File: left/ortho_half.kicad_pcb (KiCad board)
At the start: 2 copper layers, 150.9 x 146.1 mm, 60 parts, among them J1 AudioJack4, J2 Conn_01x01, J3 Conn_01x01, J4 Conn_01x01, J5 Conn_01x01, J6 Conn_01x01, J7 Conn_01x01, J8 Conn_01x01, J9 Conn_01x01, K11 KEYSW_RGB, K12 KEYSW_RGB, K13 KEYSW_RGB, K14 KEYSW_RGB, K15 KEYSW_RGB, K16 KEYSW_RGB, K21 KEYSW_RGB, K22 KEYSW_RGB, K23 KEYSW_RGB, K24 KEYSW_RGB, K25 KEYSW_RGB, K26 KEYSW_RGB, K31 KEYSW_RGB, K32 KEYSW_RGB, K33 KEYSW_RGB, K34 KEYSW_RGB, K35 KEYSW_RGB, K36 KEYSW_RGB, K41 KEYSW_RGB, K42 KEYSW_RGB, K43 KEYSW_RGB, K44 KEYSW_RGB, K45 KEYSW_RGB, K46 KEYSW_RGB, K51 KEYSW_RGB, K52 KEYSW_RGB, K53 KEYSW_RGB, K54 KEYSW_RGB, K55 KEYSW_RGB, K56 KEYSW_RGB, K61 KEYSW_RGB, K62 KEYSW_RGB, K63 KEYSW_RGB, K64 KEYSW_RGB, K65 KEYSW_RGB, K66 KEYSW_RGB, SW1 SW_PUSH_RESET, U1 EliteC, U2 IS31FL3733-TQ

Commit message: Some initial work on the PCB update.
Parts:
- added SW2: Rotary_Encoder_Switch, Keebio-Parts:RotaryEncoder_Alps_EC11E-Switch_Vertical_H20mm, F.Cu at (143.2, 111.1)
- C1, C2, C3, C4, C5, C6: footprint Capacitor_Tantalum_SMD:CP_EIA-3216-10_Kemet-I_Pad1.58x1.35mm_HandSolder -> Capacitor_SMD:C_0805_2012Metric_Pad1.15x1.40mm_HandSolder; moved to B.Cu
- R1, R2, R3, R4, R5, Rext1: footprint Keebio-Parts:Resistor-Hybrid -> Resistor_SMD:R_0603_1608Metric_Pad1.05x0.95mm_HandSolder
- U1: value EliteC -> microctrl_superset; footprint Keebio-Parts:Elite-C-castellated-24pin-holes -> vladkvit_keyb:microcontroller_eliteC_ninenano
- moved C5 17.2 mm to (136.1, 89.7)
- moved Rext1 16.3 mm to (148.7, 83.5), turned to 0 degrees
- moved R3 12.3 mm to (148.7, 82.0), turned to 180 degrees
- moved C2 11.6 mm to (136.1, 91.6)
- moved C3 10.9 mm to (136.1, 99.3)
- moved R5 8.17 mm to (148.7, 80.5), turned to 180 degrees
- moved C1 6.07 mm to (136.1, 93.5)
- moved R2 4.13 mm to (148.7, 79.0), turned to 180 degrees
- moved R4 4.06 mm to (148.7, 76.0), turned to 0 degrees
- moved C4 3.46 mm to (136.1, 95.4)
- moved C6 1.87 mm to (136.1, 97.4)
- moved R1 0.20 mm to (148.7, 77.5), turned to 180 degrees
- turned U1 to 0 degrees
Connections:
- R1 pad 1: VCC -> VIO
- U1 pad 1: col7 -> col8
- U1 pad 10: serial -> col3
- U1 pad 13: INTB -> Net-(U1-Pad13)
- U1 pad 14: row6 -> serial
- U1 pad 15: row5 -> row6
- U1 pad 16: row4 -> row5
- U1 pad 17: row3 -> row4
- U1 pad 18: row2 -> row3
- U1 pad 19: row1 -> row2
- U1 pad 2: col6 -> col7
- U1 pad 20: Net-(U1-Pad20) -> row1
- U1 pad 24: VCC -> Net-(SW3-Pad2)
- U1 pad 7: col5 -> col6
- U1 pad 8: col4 -> col5
- U1 pad 9: col3 -> col4
- U2 pad 16: led_col6 -> (no net)
- U2 pad 17: led_col5 -> (no net)
- U2 pad 18: led_col4 -> led_col6
- U2 pad 19: led_col3 -> led_col5
- U2 pad 21: led_col2 -> led_col4
- U2 pad 22: led_col1 -> led_col3
- U2 pad 23: (no net) -> led_col2
- U2 pad 24: (no net) -> led_col1
- U2 pad 25: led_col14 -> (no net)
- U2 pad 26: led_col13 -> (no net)
- U2 pad 27: led_col12 -> led_col14
- U2 pad 28: led_col11 -> led_col13
- U2 pad 30: led_col10 -> led_col12
- U2 pad 31: led_col9 -> led_col11
- U2 pad 32: (no net) -> led_col10
- U2 pad 33: (no net) -> led_col9
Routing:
- net GND: track 161.7 -> 110.8 mm, vias 45 -> 29
- net VCC: track 160.5 -> 119.6 mm, vias 1 -> 0
- net INTB: track 47.0 -> 11.2 mm, vias 1 -> 0
- net serial: track 21.8 -> 1.78 mm, vias 1 -> 0
- net Net-(Rext1-Pad1): track 22.0 -> 3.30 mm, vias 2 -> 0
- net encA2: track 0.00 -> 9.52 mm
- net encA1: track 0.00 -> 9.52 mm
- net Net-(U1-Pad27): track 0.00 -> 9.52 mm
- net SCL: track 69.2 -> 76.5 mm
- net SDA: track 77.0 -> 82.4 mm
- net col6: track 141.8 -> 138.7 mm
- net led_col4: track 113.2 -> 115.9 mm
- net led_col3: track 132.5 -> 135.2 mm
- net col4: track 165.0 -> 167.6 mm
- net col3: track 187.9 -> 190.5 mm
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
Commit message: More PCB updates
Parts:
- added J10: Conn_01x04, Connector_PinHeader_2.54mm:PinHeader_1x04_P2.54mm_Vertical, F.Cu at (159.4, 51.8)
- added J11: Conn_01x02, Connector_JST:JST_PH_S2B-PH-K_1x02_P2.00mm_Horizontal, F.Cu at (162.8, 60.4)
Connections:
- U1 pad 30: (no net) -> VBUS
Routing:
- net VCC: track 119.6 -> 92.3 mm
- net SDA: track 82.4 -> 65.9 mm
- net SCL: track 76.5 -> 63.7 mm
- net INTB: track 11.2 -> 3.99 mm
- net SDB: track 6.41 -> 3.90 mm

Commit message: More PCB stuff
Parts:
- R1, R2, R3, R4, R5, Rext1: moved to B.Cu
- SW2: footprint Keebio-Parts:RotaryEncoder_Alps_EC11E-Switch_Vertical_H20mm -> vladkvit_keyb:RotaryEncoderEC11_MX_combo
- moved J11 32.4 mm to (130.5, 59.0)
- moved J10 21.3 mm to (138.2, 53.2)
- moved C3 8.00 mm to (131.9, 92.5)
- moved Rext1 7.96 mm to (147.7, 75.6)
- moved R4 7.05 mm to (147.7, 83.0)
- moved R3 5.02 mm to (147.7, 77.0)
- moved R1 4.13 mm to (147.7, 81.5)
- moved J1 3.45 mm to (153.7, 60.0)
- moved R5 2.18 mm to (147.7, 78.5)
- moved R2 1.43 mm to (147.7, 80.0)
- moved SW2 0.45 mm to (143.5, 110.7)
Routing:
- net SDA: track 65.9 -> 71.5 mm
- net GND: track 110.5 -> 115.9 mm
- net SCL: track 63.7 -> 69.1 mm
- net VCC: track 92.3 -> 95.0 mm
- net VIO: track 67.4 -> 65.5 mm, vias 4 -> 0
- net row6: track 254.3 -> 255.7 mm
- net col1: track 228.9 -> 228.2 mm
- net row5: track 187.9 -> 188.6 mm
- net led_row3B: track 389.1 -> 388.4 mm
- net row4: track 170.0 -> 170.7 mm
- net led_row3A: track 403.3 -> 402.7 mm
- net led_row3C: track 379.4 -> 378.9 mm

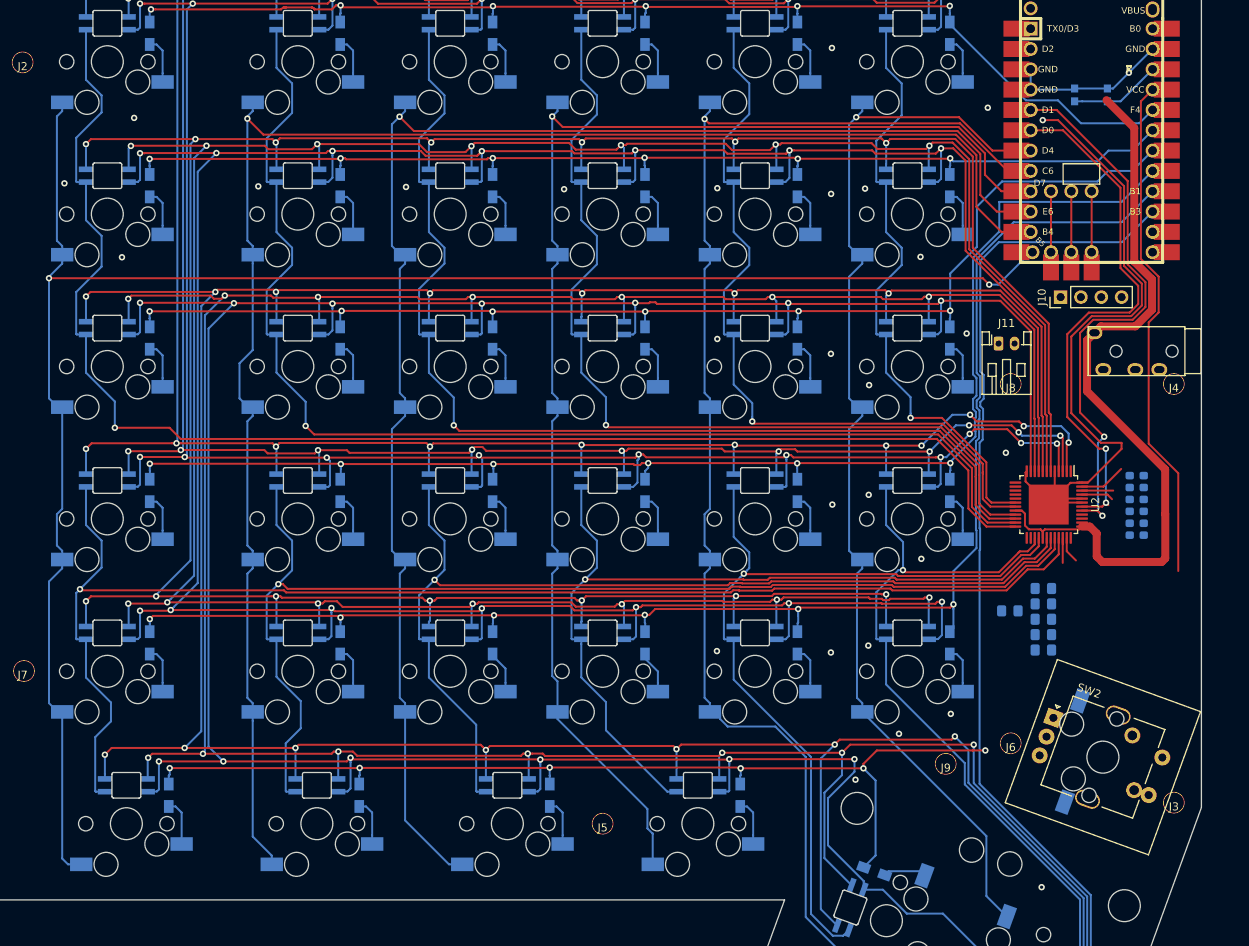
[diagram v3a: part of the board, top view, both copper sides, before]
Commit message: A bunch of changes to left half of PCB in order to make room for battery and various connectors. Also added a switch and extra connector on the schematic.
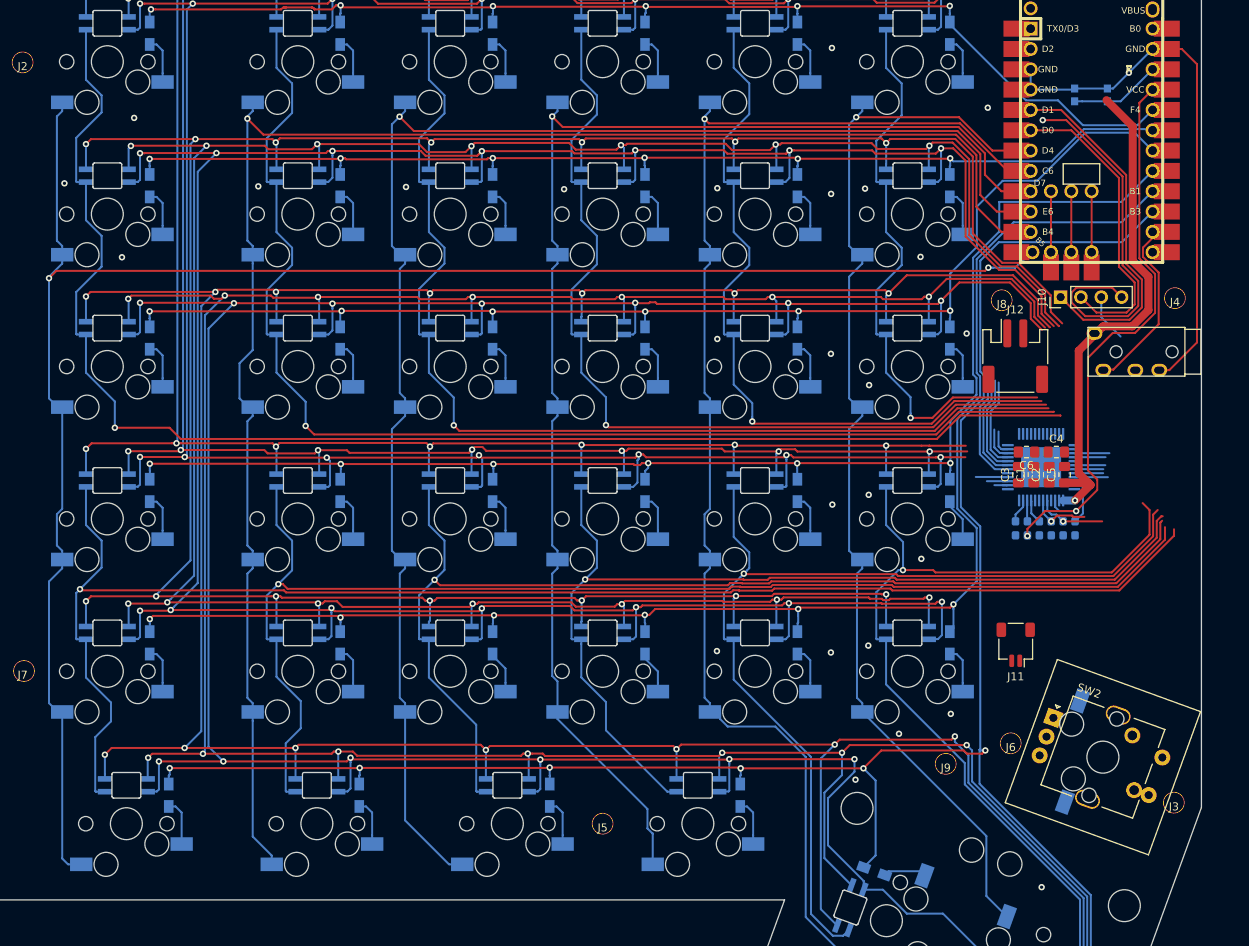
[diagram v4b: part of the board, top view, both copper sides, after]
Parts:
- added J12: Conn_01x02, Connector_JST:JST_PH_S2B-PH-SM4-TB_1x02-1MP_P2.00mm_Horizontal, F.Cu at (132.5, 60.6)
- C1, C2, C3, C4, C5, C6: moved to F.Cu
- J11: footprint Connector_JST:JST_PH_S2B-PH-K_1x02_P2.00mm_Horizontal -> Connector_JST:JST_SH_SM02B-SRSS-TB_1x02-1MP_P1.00mm_Horizontal
- U2: moved to B.Cu
- moved J11 37.7 mm to (132.6, 96.7), turned to 180 degrees
- moved C6 24.8 mm to (133.9, 72.6), turned to 180 degrees
- moved C4 22.9 mm to (137.7, 72.6)
- moved C1 18.1 mm to (134.9, 75.4), turned to 90 degrees
- moved C3 17.1 mm to (132.9, 75.4), turned to 90 degrees
- moved C2 16.2 mm to (136.8, 75.4), turned to 90 degrees
- moved R4 15.2 mm to (132.6, 82.1), turned to 270 degrees
- moved C5 14.5 mm to (138.7, 75.4), turned to 90 degrees
- moved R1 13.7 mm to (134.1, 82.1), turned to 90 degrees
- moved R2 12.4 mm to (135.6, 82.1), turned to 90 degrees
- moved R5 11.3 mm to (137.0, 82.1), turned to 90 degrees
- moved J4 10.7 mm to (152.5, 53.4)
- moved J8 10.5 mm to (130.8, 53.6)
- moved R3 10.5 mm to (138.5, 82.1), turned to 90 degrees
- moved Rext1 10.1 mm to (140.0, 82.1), turned to 270 degrees
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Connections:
- J11 pad 2: VBUS -> Net-(J11-Pad2)
- SW2 pad S1: (no net) -> col7
- SW2 pad S2: (no net) -> row6
- U1 pad 30: VBUS -> (no net)
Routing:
- net VCC: track 95.0 -> 64.2 mm, vias 0 -> 1
- net led_col14: track 92.9 -> 115.7 mm
- net serial: track 1.78 -> 23.9 mm
- net SCL: track 69.1 -> 47.4 mm, vias 2 -> 1
- net led_col13: track 106.5 -> 127.7 mm
- net led_col12: track 107.7 -> 127.8 mm
- net led_col11: track 125.8 -> 144.7 mm
- net led_row1A: track 329.2 -> 310.7 mm, vias 18 -> 14
- net led_col9: track 171.5 -> 189.8 mm
- net led_col10: track 145.6 -> 163.7 mm
- net SDA: track 71.5 -> 55.1 mm, vias 2 -> 1
- net led_row1B: track 319.7 -> 304.0 mm, vias 17 -> 14
- net VIO: track 65.5 -> 80.1 mm, vias 0 -> 2
- net led_row1C: track 342.1 -> 328.9 mm, vias 17 -> 14
- net led_row3B: track 388.4 -> 378.3 mm
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
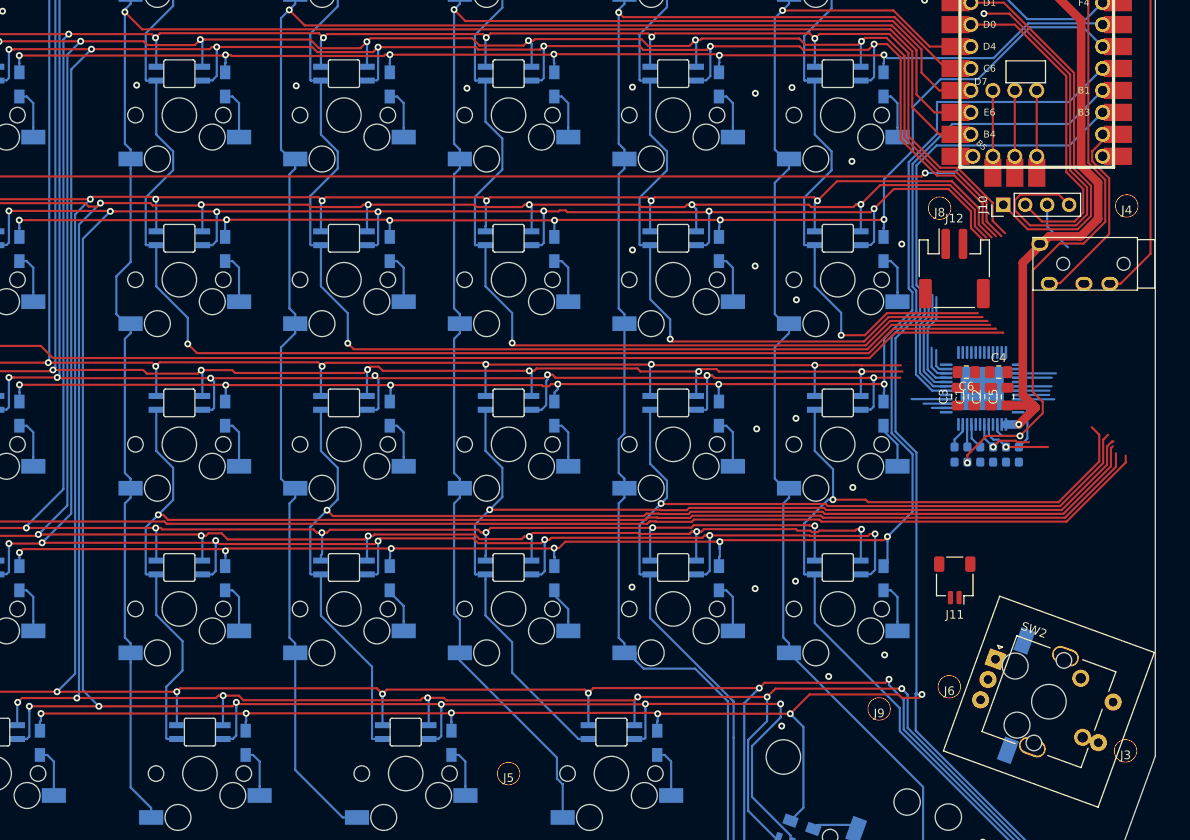
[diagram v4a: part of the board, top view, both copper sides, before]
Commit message: Moved around components and placed the JST power connectors
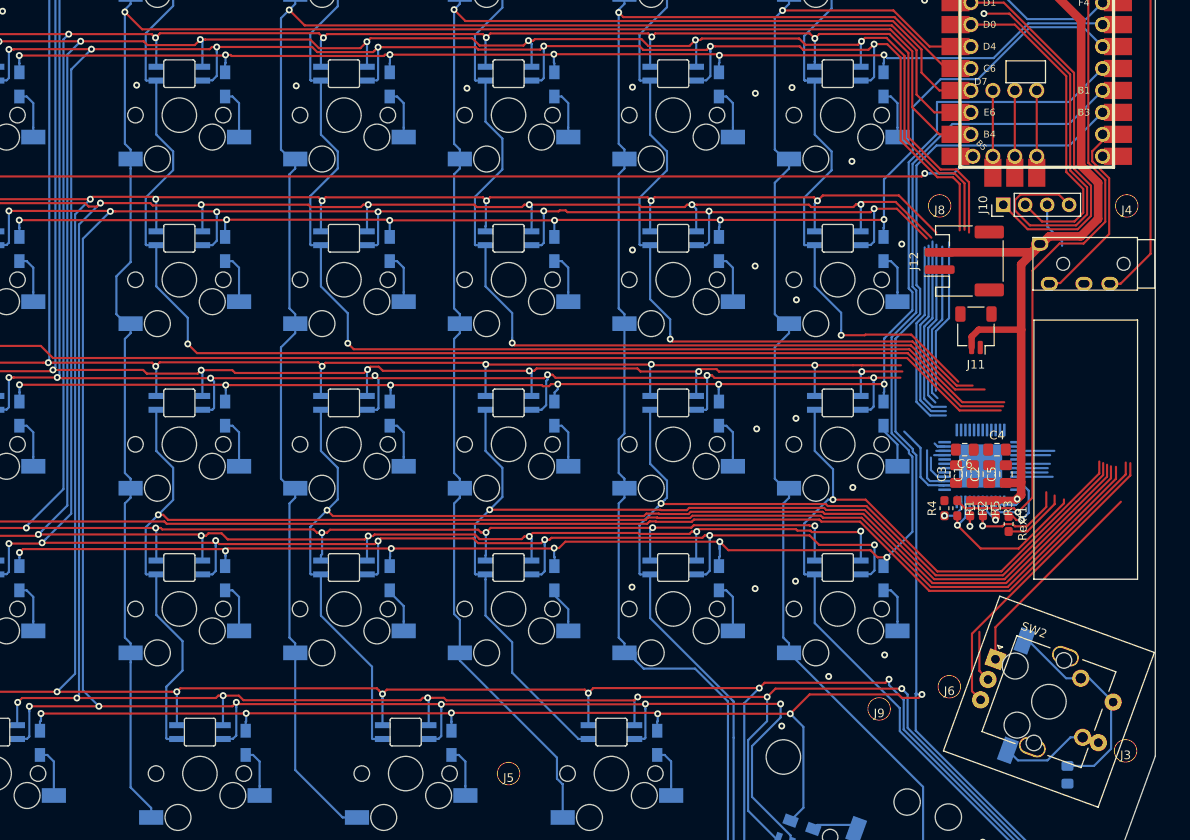
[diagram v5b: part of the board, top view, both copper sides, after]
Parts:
- added D1: DIODE, Diode_SMD:D_0805_2012Metric_Pad1.15x1.40mm_HandSolder, B.Cu at (145.6, 119.2)
- R1, R2, R3, R4, R5, Rext1: moved to F.Cu
- moved J11 29.0 mm to (135.1, 67.8)
- moved C1 8.97 mm to (134.7, 84.4)
- moved C2 8.97 mm to (136.6, 84.4)
- moved C3 8.97 mm to (132.8, 84.4)
- moved C4 8.97 mm to (137.5, 81.6)
- moved C5 8.97 mm to (138.5, 84.4)
- moved C6 8.97 mm to (133.8, 81.6)
- moved U2 8.97 mm to (135.6, 83.5)
- moved Rext1 8.11 mm to (138.8, 90.2)
- moved R3 6.32 mm to (137.4, 88.4), turned to 270 degrees
- moved R5 6.32 mm to (135.9, 88.4), turned to 270 degrees
- moved R2 6.32 mm to (134.4, 88.4), turned to 270 degrees
- moved R1 6.32 mm to (132.9, 88.4), turned to 270 degrees
- moved R4 6.32 mm to (131.4, 88.4), turned to 90 degrees
- moved J12 1.44 mm to (133.7, 59.7), turned to 90 degrees
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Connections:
- J11 pad 2: Net-(J11-Pad2) -> VCC
- J11 pad MP: (no net) -> GND
- J12 pad 2: Net-(J11-Pad2) -> VCC
- J12 pad MP: (no net) -> GND
- SW2 pad S2: row6 -> Net-(D1-Pad1)
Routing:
- net encA2: track 9.52 -> 44.9 mm
- net VCC: track 64.2 -> 95.3 mm
- net Net-(D1-Pad1): track 0.00 -> 24.6 mm
- net encA1: track 9.52 -> 33.8 mm
- net SDB: track 2.62 -> 20.3 mm, vias 0 -> 1
- net GND: track 118.4 -> 132.0 mm
- net col7: track 1.78 -> 14.1 mm
- net led_row1A: track 310.7 -> 318.2 mm
- net VIO: track 80.1 -> 87.2 mm, vias 2 -> 1
- net SCL: track 47.4 -> 54.0 mm
- net led_col9: track 189.8 -> 196.4 mm
- net led_row3C: track 368.9 -> 375.2 mm
- net led_row2A: track 356.9 -> 363.1 mm
- net led_row3B: track 378.3 -> 384.3 mm
- net led_col10: track 163.7 -> 169.5 mm
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
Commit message: Lots of changes to left side of controller. Should be pretty close to rev2
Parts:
- added J13: Conn_01x01, vladkvit_keyb:standoff_m2.5, F.Cu at (31.1, 33.4)
- added J14: Conn_01x01, vladkvit_keyb:standoff_m2.5, F.Cu at (135.9, 60.3)
- added J15: Conn_01x01, vladkvit_keyb:standoff_m2.5, F.Cu at (30.9, 90.5)
- added J16: Conn_01x01, vladkvit_keyb:standoff_m2.5, F.Cu at (106.6, 112.4)
- added J17: Conn_01x01, vladkvit_keyb:SMTSO_mount_m2.5, B.Cu at (90.5, 52.4)
- added SW4: SW_SPST, Jumper:SolderJumper-2_P1.3mm_Open_RoundedPad1.0x1.5mm, B.Cu at (139.7, 23.6)
- added SW5: SW_SPST, Jumper:SolderJumper-2_P1.3mm_Open_RoundedPad1.0x1.5mm, B.Cu at (142.2, 23.6)
- added SW6: SW_SPST, Jumper:SolderJumper-2_P1.3mm_Open_RoundedPad1.0x1.5mm, B.Cu at (144.7, 23.6)
- J1: footprint vladkvit_keyb:TRRS-PJ-320A -> vladkvit_keyb:TRRS-PJ-320D
- J11: value Conn_01x02 -> Conn_01x01; footprint Connector_JST:JST_SH_SM02B-SRSS-TB_1x02-1MP_P1.00mm_Horizontal -> vladkvit_keyb:SMTSO_mount_m2.5; moved to B.Cu
- J12: footprint Connector_JST:JST_PH_S2B-PH-SM4-TB_1x02-1MP_P2.00mm_Horizontal -> vladkvit_keyb:battery_solder_point
- J2, J3, J5, J6, J7, J9: footprint vladkvit_keyb:m2.5_hole -> vladkvit_keyb:SMTSO_mount_m2.5; moved to B.Cu
- moved J3 118.7 mm to (52.4, 52.4)
- moved J9 114.3 mm to (9.59, 109.4)
- moved J6 75.2 mm to (57.1, 116.0)
- moved J11 37.1 mm to (131.8, 104.7), turned to 0 degrees
- moved J7 28.6 mm to (9.60, 71.4)
- moved J12 11.2 mm to (136.3, 70.6), turned to 0 degrees
- moved J2 9.66 mm to (10.4, 33.4)
- moved J5 3.47 mm to (80.9, 115.6)
- moved J8 2.16 mm to (133.0, 53.2)
- moved J4 1.35 mm to (151.2, 53.2)
- moved J10 0.05 mm to (138.3, 53.2)
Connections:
- J3 pad 1: (no net) -> GND
- J4 pad 1: (no net) -> GND
- J6 pad 1: (no net) -> GND
- J8 pad 1: (no net) -> GND
- U1 pad 30: (no net) -> VBUS
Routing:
- net GND: track 132.0 -> 295.6 mm, vias 28 -> 40
- net col7: track 14.1 -> 124.6 mm, vias 0 -> 4
- net encA2: track 44.9 -> 99.2 mm, vias 0 -> 1
- net encA1: track 33.8 -> 84.8 mm, vias 0 -> 1
- net SDA: track 49.4 -> 91.0 mm, vias 1 -> 4
- net SCL: track 54.0 -> 89.8 mm, vias 1 -> 2
- net led_row3B: track 384.3 -> 415.3 mm, vias 14 -> 15
- net led_row3A: track 400.0 -> 430.7 mm, vias 14 -> 15
- net VCC: track 95.3 -> 125.4 mm, vias 1 -> 5
- net led_row3C: track 375.2 -> 404.6 mm, vias 13 -> 14
- net row6: track 258.0 -> 286.2 mm, vias 6 -> 8
- net row4: track 170.4 -> 187.0 mm, vias 6 -> 8
- net SDB: track 20.3 -> 4.20 mm
- net led_row1C: track 328.3 -> 342.0 mm, vias 14 -> 15
- net led_row1A: track 318.2 -> 331.9 mm, vias 14 -> 15
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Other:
- outline, holes or cut-outs redrawn
- board text added: "301230 Only for compatible microcontrollers"
- board text added: "GND"

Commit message: Minor updates
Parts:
- turned J12 to 90 degrees
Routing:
- net VCC: track 125.4 -> 121.2 mm
- net GND: track 295.6 -> 298.9 mm, vias 40 -> 106
- net led_row3A: track 430.7 -> 427.9 mm
- net row3: track 160.3 -> 158.0 mm
- net led_row3B: track 415.3 -> 413.5 mm
- net row1: track 145.8 -> 144.5 mm
- net row6: track 286.2 -> 287.3 mm
- net row2: track 143.5 -> 142.6 mm
- net col3: track 189.5 -> 190.3 mm
- net led_row1A: track 331.9 -> 332.7 mm
- net col7: track 124.6 -> 125.2 mm
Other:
- outline, holes or cut-outs redrawn
- board text added: "Elite C/ VBUS"
- board text added: "Pro Micro/ RAW"
- board text added: "RESET"
- board text added: "Voltage Jumper"
- board text added: "nice!nano/ VCC"
